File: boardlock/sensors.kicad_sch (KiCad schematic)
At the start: 33 parts, among them Q2 MMBT4401, Q4 BSS84PWH6327XTSA1, U1 LSM6DSO32, U3 SAM-M8Q

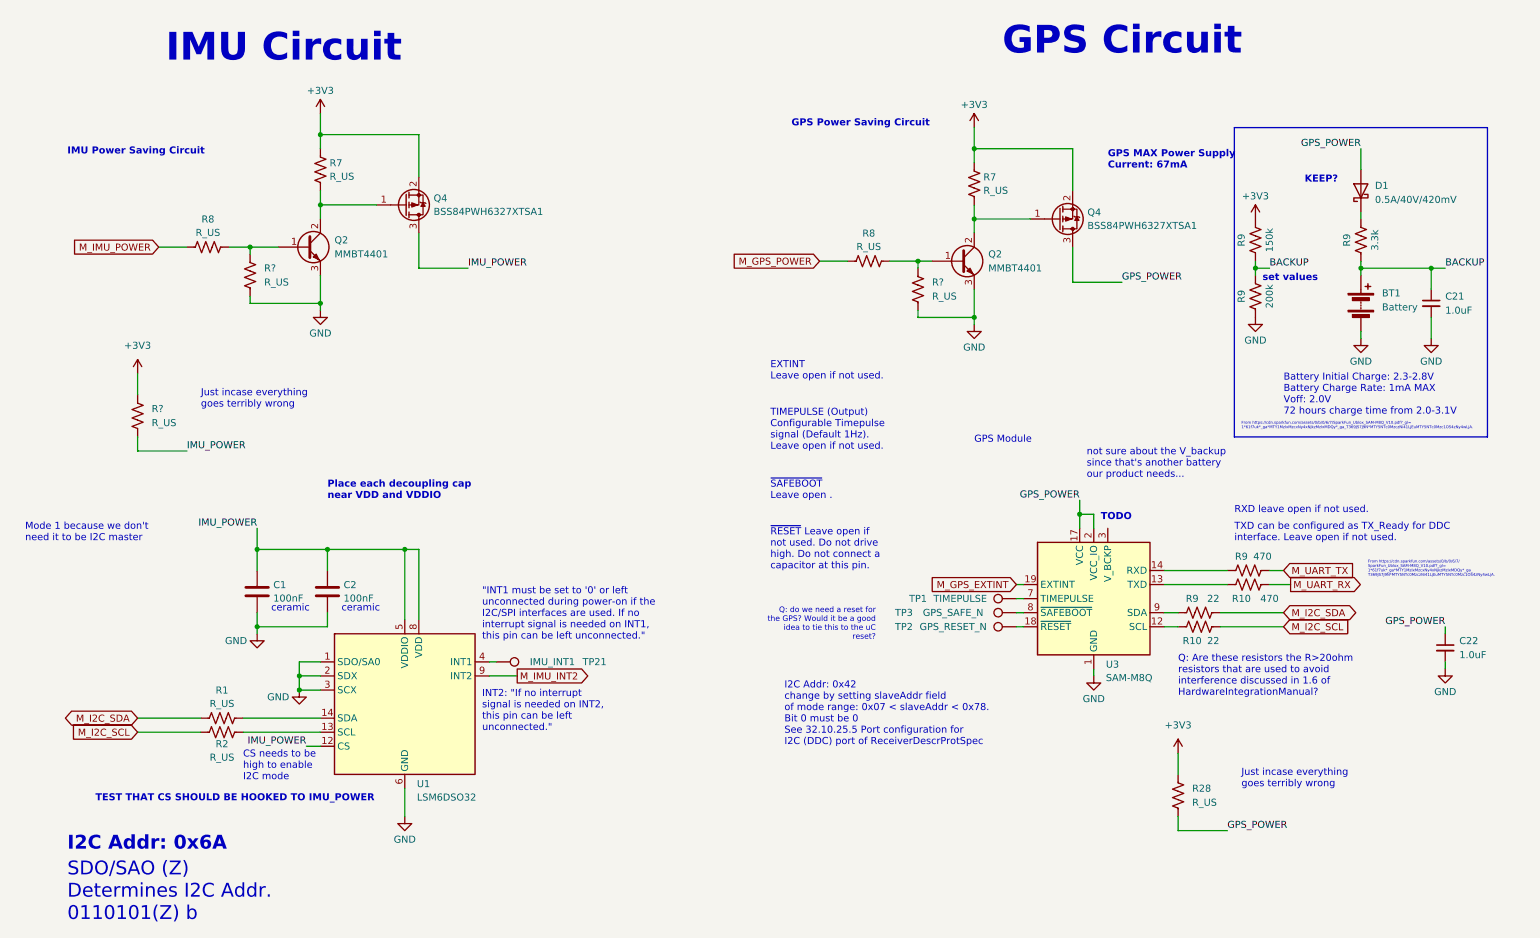
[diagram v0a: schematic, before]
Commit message: delete misc, add testpoints, add sensor signals to micro
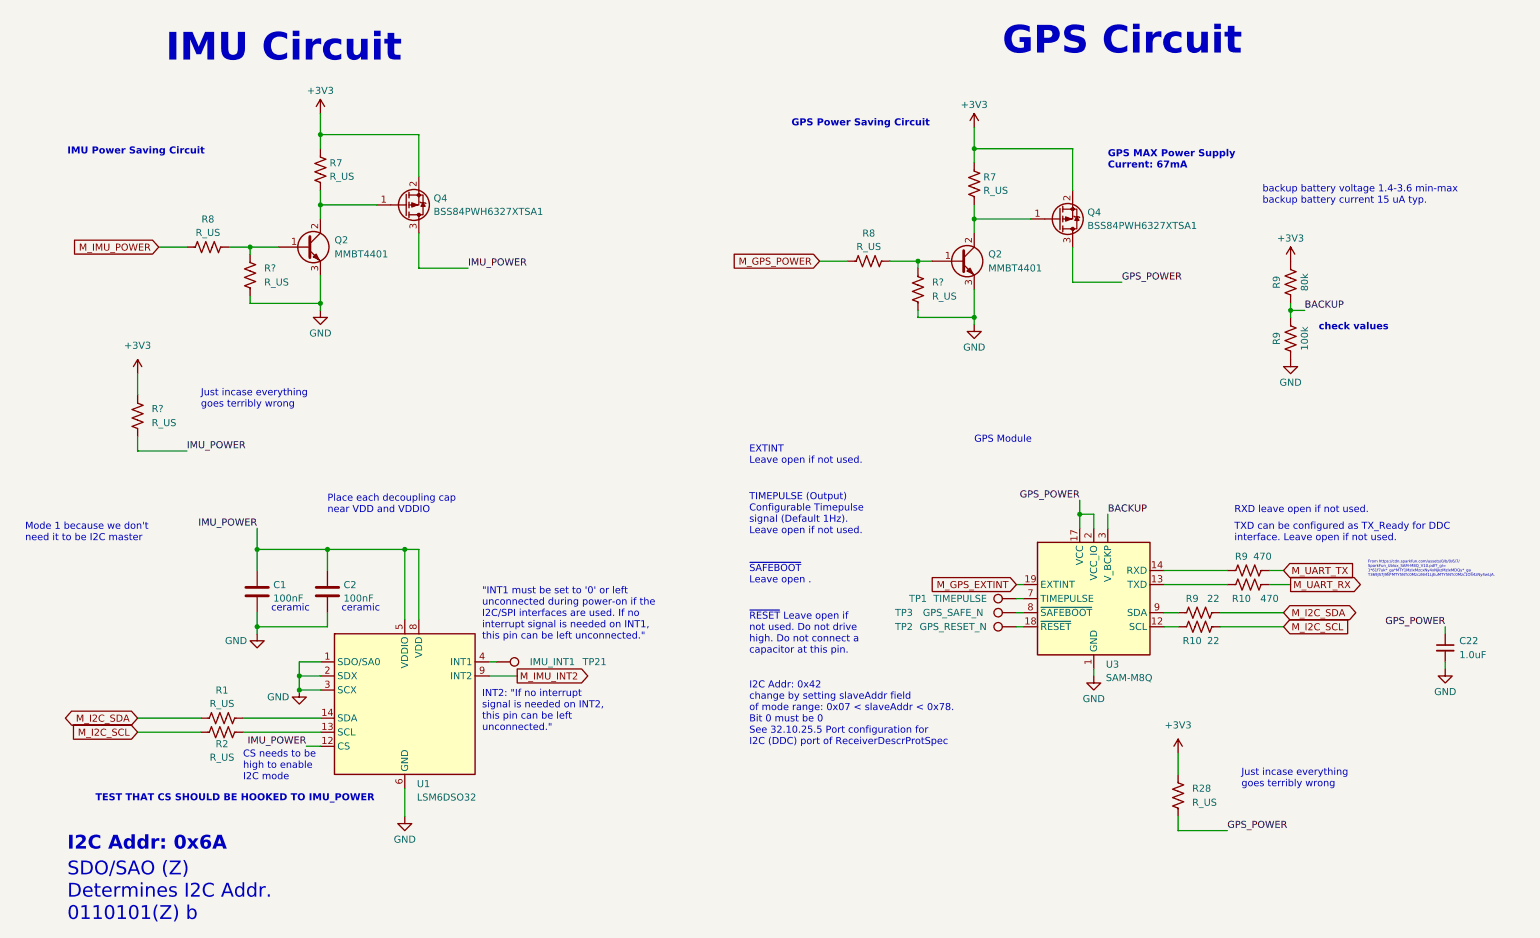
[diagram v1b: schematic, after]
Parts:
- removed BT1: Battery, symbol Device:Battery
- removed C21: 1.0uF, symbol Device:C_Small
- removed D1: 0.5A/40V/420mV, symbol Device:D_Schottky
- removed R9: 3.3k, symbol Device:R_US
- R9: value 150k -> 80k
- R9: value 200k -> 100k
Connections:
- net BACKUP: now also U3.3 (V_BCKP)
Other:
- note added: "backup battery voltage 1.4-3.6 min-max backup battery current 15 uA typ."
- note added: "check values"
- note removed: "Battery Initial Charge: 2.3-2.8V Battery Charge Rate: 1mA MAX Voff: 2.0V 72 hours charge time from 2.0-3.1V"
- note removed: "From https://cdn.sparkfun.com/assets/0/b/0/6/7/SparkFun_Ublox_SAM-M8Q_V10.pdf?_gl= 1*61f7uk*_ga*MTY1MzIxMzcxNy4xNjkzMzIxMDQy*_ga_T369JS7J9N*MTY5NTc0MzczNi41LjEuMTY5NTc0Mzc1OS4zNy4wLjA."
- note removed: "KEEP?"
- note removed: "Q: Are these resistors the R>20ohm resistors that are used to avoid interference discussed in 1.6 of HardwareIntegrationManual?"
- note removed: "Q: do we need a reset for the GPS? Would it be a good idea to tie this to the uC reset?"
- note removed: "TODO"
- note removed: "not sure about the V_backup since that's another battery our product needs..."
- note removed: "set values"
- moved on the sheet: R9

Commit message: footprint work
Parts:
- added C35: 1.0uF, Capacitor_SMD:C_0805_2012Metric_Pad1.18x1.45mm_HandSolder, symbol Device:C_Small
- C1, C2, C22: footprint (none) -> Capacitor_SMD:C_0805_2012Metric_Pad1.18x1.45mm_HandSolder
- Q2: footprint (none) -> Package_TO_SOT_SMD:SOT-23-3
- R1, R10, R2, R28, R7, R8, R9: footprint (none) -> Resistor_SMD:R_0805_2012Metric_Pad1.20x1.40mm_HandSolder
- R24, R25, R38: renamed from R?; footprint (none) -> Resistor_SMD:R_0805_2012Metric_Pad1.20x1.40mm_HandSolder
- TP1, TP2, TP21, TP3: footprint (none) -> TestPoint:TestPoint_Plated_Hole_D3.0mm
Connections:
- net BACKUP: now also C35.1
- net GND: now also C35.2

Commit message: changes
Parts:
- removed C35: 1.0uF, Capacitor_SMD:C_0805_2012Metric_Pad1.18x1.45mm_HandSolder, symbol Device:C_Small
- removed R9: 80k, Resistor_SMD:R_0805_2012Metric_Pad1.20x1.40mm_HandSolder, symbol Device:R_US
- removed R9: 100k, Resistor_SMD:R_0805_2012Metric_Pad1.20x1.40mm_HandSolder, symbol Device:R_US
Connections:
- net BACKUP is gone; now on net +3V3: U3.3 (V_BCKP)
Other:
- note removed: "check values"

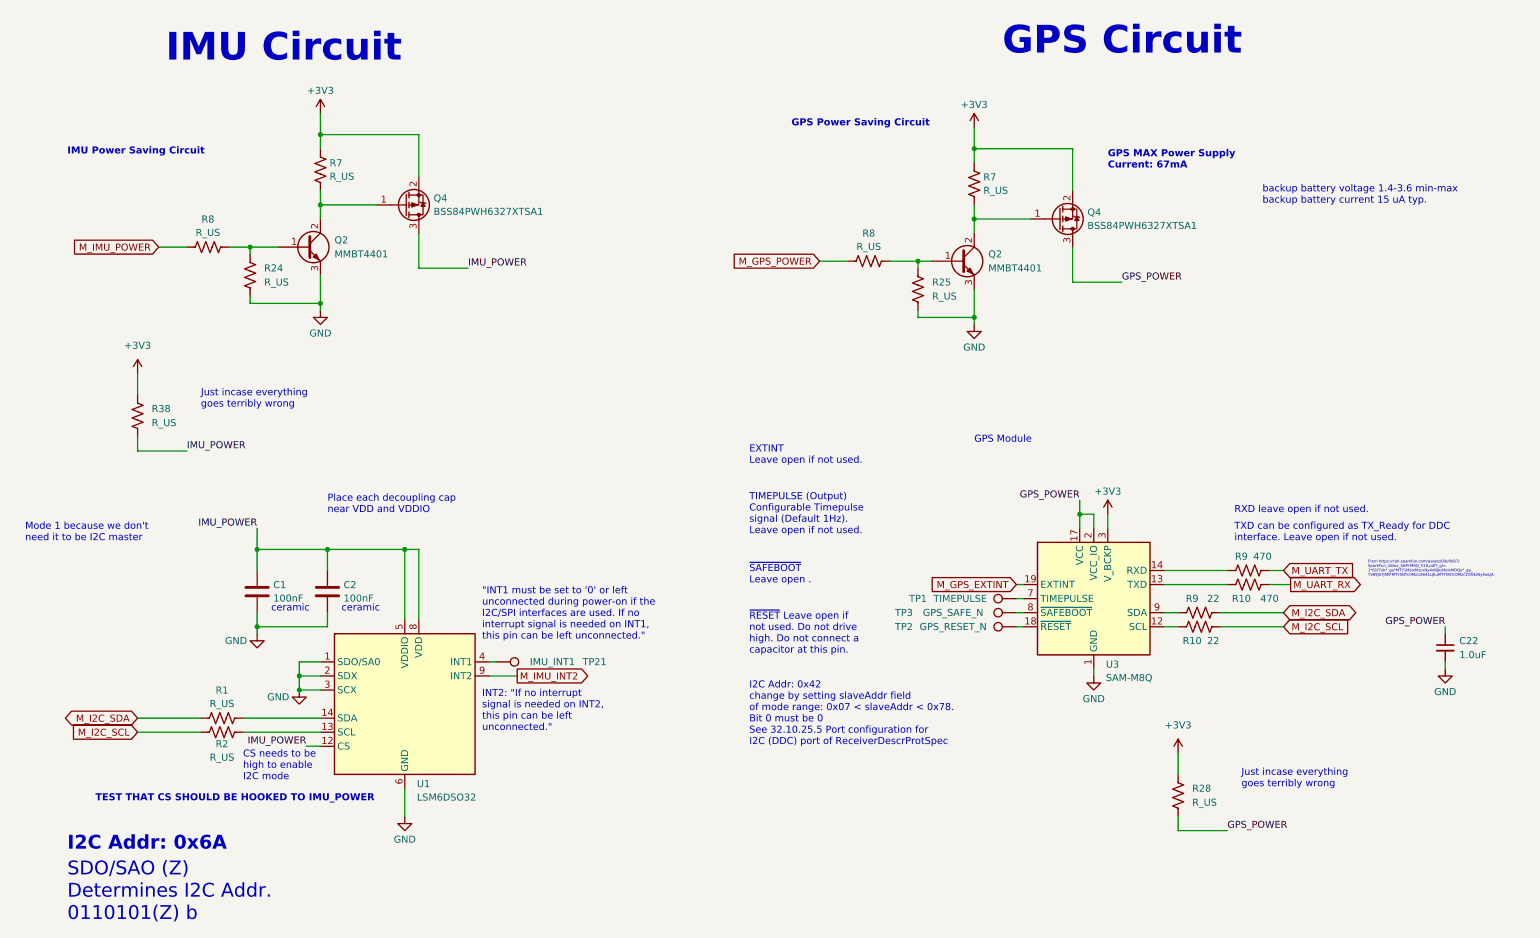
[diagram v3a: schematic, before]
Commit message: correcting old schematic and footprints
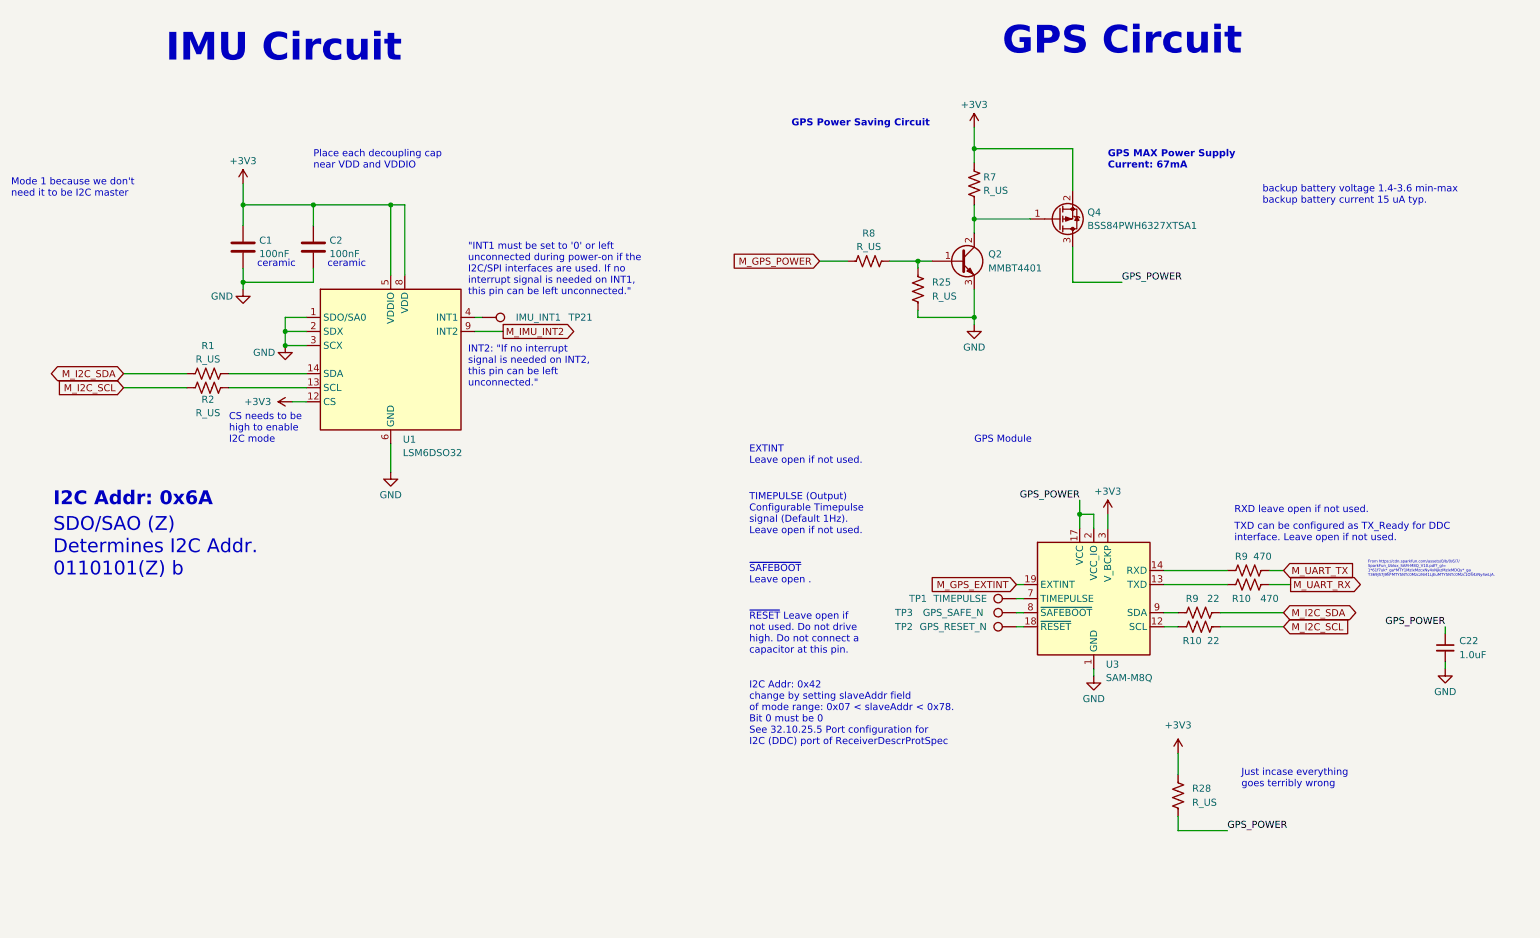
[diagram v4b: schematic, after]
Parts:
- removed Q2: MMBT4401, Package_TO_SOT_SMD:SOT-23-3, symbol Device:Q_NPN_BCE
- removed Q4: BSS84PWH6327XTSA1, Package_TO_SOT_SMD:SOT-323_SC-70_Handsoldering, symbol Device:Q_PMOS_GSD
- removed R24, R38, R7, R8: R_US, Resistor_SMD:R_0805_2012Metric_Pad1.20x1.40mm_HandSolder, symbol Device:R_US
- TP1, TP2, TP21, TP3: footprint TestPoint:TestPoint_Plated_Hole_D3.0mm -> TestPoint:TestPoint_Pad_D1.0mm
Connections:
- net IMU_POWER is gone; now on net +3V3: C1.1, C2.1, U1.12 (CS), U1.5 (VDDIO), U1.8 (VDD)
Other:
- note removed: "IMU Power Saving Circuit"
- note removed: "TEST THAT CS SHOULD BE HOOKED TO IMU_POWER"
- moved on the sheet: C1, C2, R1, R2, TP21, U1

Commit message: pcb work
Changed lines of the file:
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@@
     (effects (font (size 1.27 1.27)) (justify left bottom))
-  )
-  (label "GPS_POWER" (at 276.86 124.46 180) (fields_autoplaced)
-    (effects (font (size 1.27 1.27)) (justify right bottom))
-  )
-  (label "GPS_POWER" (at 237.49 161.29 0) (fields_autoplaced)
-    (effects (font (size 1.27 1.27)) (justify left bottom))
-  )
-  (label "GPS_POWER" (at 218.44 62.23 0) (fields_autoplaced)
-    (effects (font (size 1.27 1.27)) (justify left bottom))
-  )
-  (label "GPS_POWER" (at 210.82 101.6 180) (fields_autoplaced)
-    (effects (font (size 1.27 1.27)) (justify right bottom))
   )
   (global_label "M_UART_TX" (shape input) (at 247.65 114.3 0) (fields_autoplaced)
@@
     (property "Intersheetrefs" "${INTERSHEET_REFS}" (at 260.8556 114.3 0)
       (effects (font (size 1.27 1.27)) (justify left) hide)
+    )
+  )
+  (global_label "GPS_POWER" (shape input) (at 210.82 101.6 180) (fields_autoplaced)
+    (effects (font (size 1.27 1.27)) (justify right))
+    (property "Intersheetrefs" "${INTERSHEET_REFS}" (at 196.6468 101.6 0)
+      (effects (font (size 1.27 1.27)) (justify right) hide)
     )
   )
@@
     )
   )
+  (global_label "GPS_POWER" (shape output) (at 218.44 62.23 0) (fields_autoplaced)
+    (effects (font (size 1.27 1.27)) (justify left))
+    (property "Intersheetrefs" "${INTERSHEET_REFS}" (at 232.6132 62.23 0)
+      (effects (font (size 1.27 1.27)) (justify left) hide)
+    )
+  )
   (global_label "M_I2C_SDA" (shape bidirectional) (at 247.65 121.92 0) (fields_autoplaced)
     (effects (font (size 1.27 1.27)) (justify left))
     (property "Intersheetrefs" "${INTERSHEET_REFS}" (at 261.7061 121.92 0)
+      (effects (font (size 1.27 1.27)) (justify left) hide)
+    )
+  )
+  (global_label "GPS_POWER" (shape output) (at 237.49 161.29 0) (fields_autoplaced)
+    (effects (font (size 1.27 1.27)) (justify left))
+    (property "Intersheetrefs" "${INTERSHEET_REFS}" (at 251.6632 161.29 0)
       (effects (font (size 1.27 1.27)) (justify left) hide)
     )
@@
       (effects (font (size 1.27 1.27)) (justify right) hide)
     )
+  )
+  (global_label "GPS_POWER" (shape input) (at 276.86 124.46 180) (fields_autoplaced)
+    (effects (font (size 1.27 1.27)) (justify right))
+    (property "Intersheetrefs" "${INTERSHEET_REFS}" (at 262.6868 124.46 0)
+      (effects (font (size 1.27 1.27)) (justify right) hide)
+    )
